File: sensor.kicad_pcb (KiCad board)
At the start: 2 copper layers, 62 x 58.5 mm, 7 parts, among them U1 ESP-12F

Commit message: Schematic finishing and cleanup.
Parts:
- renumbered REF** to CON1, U1 to U3, REF** to U5
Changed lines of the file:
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@@
     (tags "Micro-USB SMD Typ-B")
     (attr smd)
-    (fp_text reference REF** (at 0 -3.1125) (layer F.SilkS)
+    (fp_text reference CON1 (at 0 -3.1125) (layer F.SilkS)
       (effects (font (size 1 1) (thickness 0.15)))
     )
@@
     (tags "Wi-Fi Module")
     (attr smd)
-    (fp_text reference U1 (at -10.56 -5.26) (layer F.SilkS)
+    (fp_text reference U3 (at -10.56 -5.26) (layer F.SilkS)
       (effects (font (size 1 1) (thickness 0.15)))
     )
@@
     (descr "Through hole straight socket strip, 2x05, 1.27mm pitch, double cols (from Kicad 4.0.7), script generated")
     (tags "Through hole socket strip THT 2x05 1.27mm double row")
-    (fp_text reference REF** (at 0 8.89) (layer B.SilkS)
+    (fp_text reference U5 (at 0 8.89) (layer B.SilkS)
       (effects (font (size 1 1) (thickness 0.15)) (justify mirror))
     )

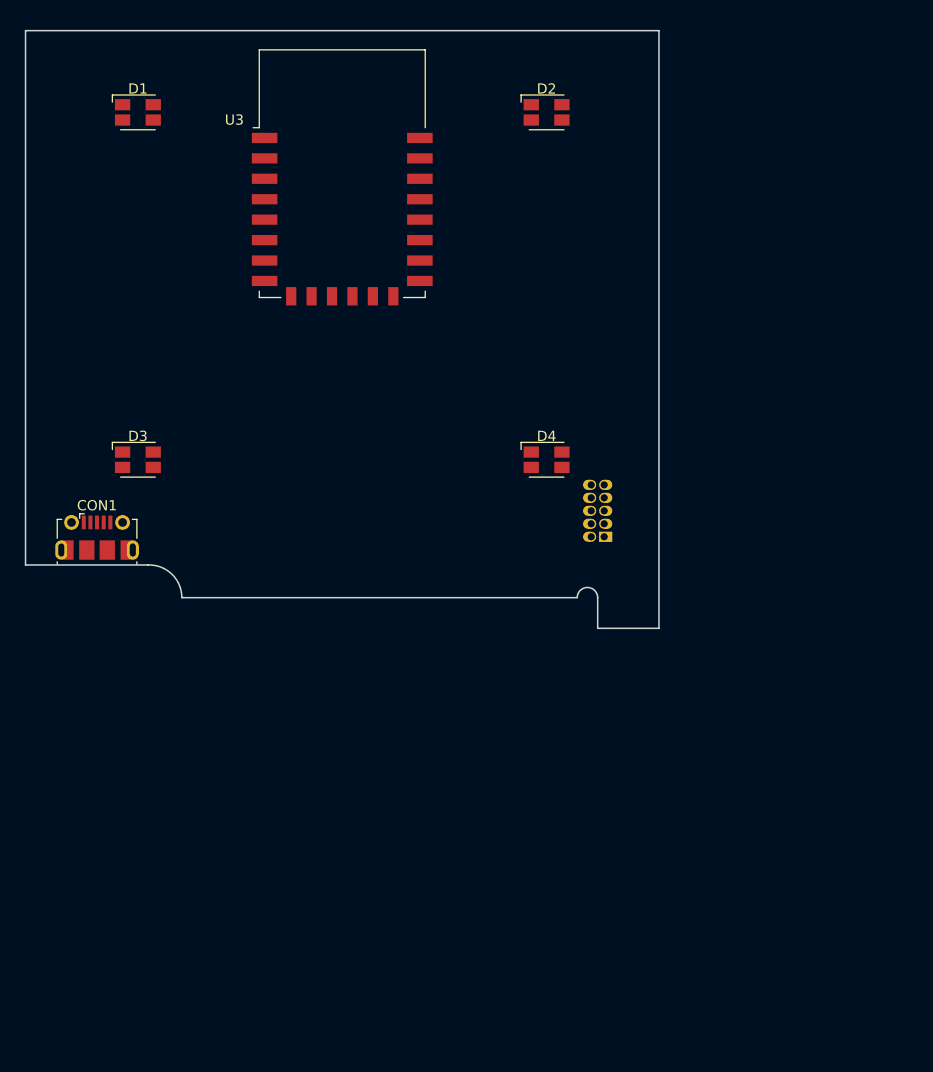
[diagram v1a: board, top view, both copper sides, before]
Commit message: Initial draft PCB placement
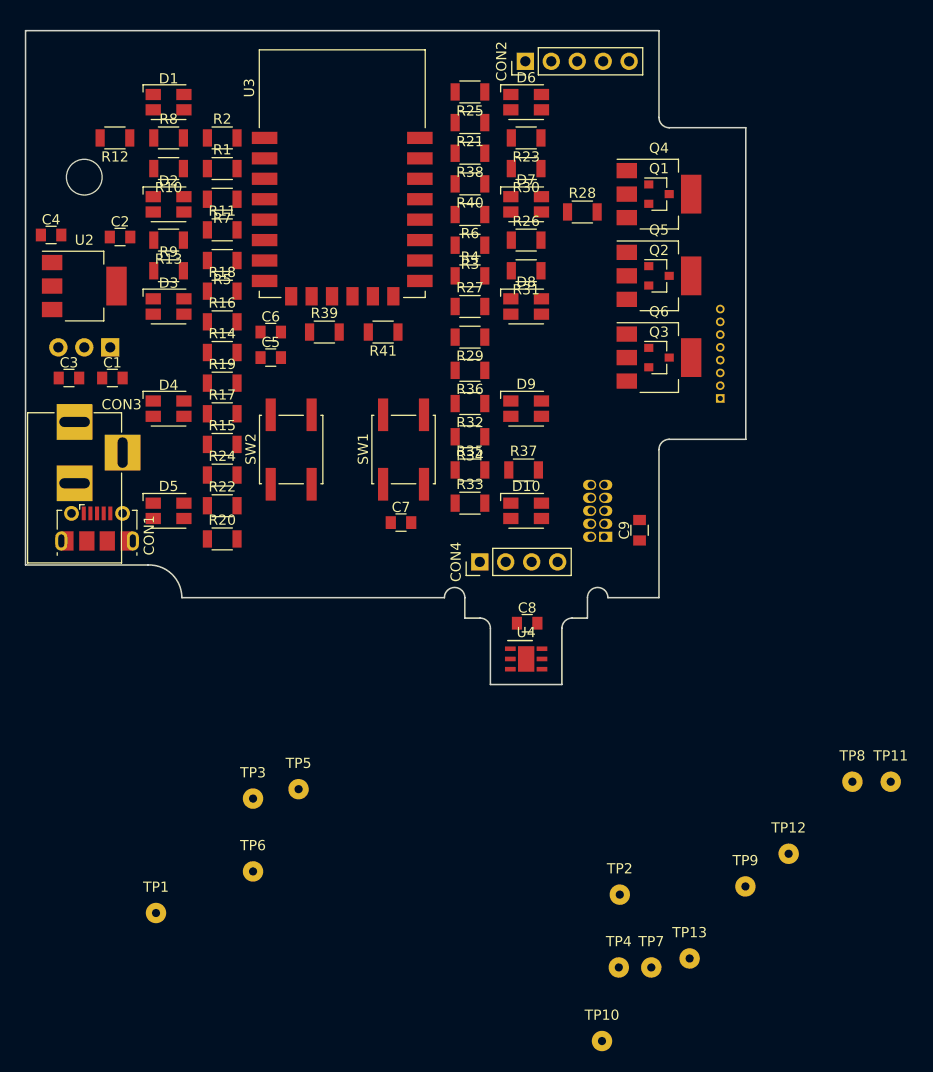
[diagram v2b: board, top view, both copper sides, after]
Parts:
- added C1: 1uF/25V, Capacitors_SMD:C_0805, F.Cu at (74.5, 76.0)
- added C2: 10uF/10V, Capacitors_SMD:C_0805, F.Cu at (75.2, 62.2)
- added C3: 100nF, Capacitors_SMD:C_0805, F.Cu at (70.2, 76.0)
- added C4: 10uF/10V, Capacitors_SMD:C_0805, F.Cu at (68.5, 62.0)
- added C5: 10uF/10V, Capacitors_SMD:C_0805, F.Cu at (90.0, 74.0)
- added C6: 100nF, Capacitors_SMD:C_0805, F.Cu at (90.0, 71.5)
- added C7: 100nF, Capacitors_SMD:C_0805, F.Cu at (102.8, 90.2)
- added C8: 100nF, Capacitors_SMD:C_0805, F.Cu at (115.1, 100.0)
- added C9: 10uF/10V, Capacitors_SMD:C_0805, F.Cu at (126.1, 90.9)
- added CON2: PROG, Pin_Headers:Pin_Header_Straight_1x05_Pitch2.54mm, F.Cu at (114.9, 45.0)
- added CON3: Jack-DC, Connectors:BARREL_JACK, F.Cu at (70.8, 80.3)
- added CON4: HTU21D, Pin_Headers:Pin_Header_Straight_1x04_Pitch2.54mm, F.Cu at (110.5, 94.0)
- added CON5: Conn_01x08, Connectors_Molex:Molex_PicoBlade_53048-0810_08x1.25mm_Angled, B.Cu at (134.0, 78.0)
- added D10: ASMB-MTB0-0A3A2, less-smog:ASMB-MTB0-0A3A2, F.Cu at (115.0, 89.0)
- added D5: ASMB-MTB0-0A3A2, less-smog:ASMB-MTB0-0A3A2, F.Cu at (80.0, 89.0)
- added D6: ASMB-MTB0-0A3A2, less-smog:ASMB-MTB0-0A3A2, F.Cu at (115.0, 49.0)
- added D7: ASMB-MTB0-0A3A2, less-smog:ASMB-MTB0-0A3A2, F.Cu at (115.0, 59.0)
- added D8: ASMB-MTB0-0A3A2, less-smog:ASMB-MTB0-0A3A2, F.Cu at (115.0, 69.0)
- added D9: ASMB-MTB0-0A3A2, less-smog:ASMB-MTB0-0A3A2, F.Cu at (115.0, 79.0)
- added Q1: BSS214N, TO_SOT_Packages_SMD:SOT-23, F.Cu at (128.0, 58.0)
- added Q2: BSS214N, TO_SOT_Packages_SMD:SOT-23, F.Cu at (128.0, 66.0)
- added Q3: BSS214N, TO_SOT_Packages_SMD:SOT-23, F.Cu at (128.0, 74.0)
- added Q4: BSS214N, TO_SOT_Packages_SMD:SOT-223-3Lead_TabPin2, F.Cu at (128.0, 58.0)
- added Q5: BSS214N, TO_SOT_Packages_SMD:SOT-223-3Lead_TabPin2, F.Cu at (128.0, 66.0)
- added Q6: BSS214N, TO_SOT_Packages_SMD:SOT-223-3Lead_TabPin2, F.Cu at (128.0, 74.0)
- added R1: 10k, Resistors_SMD:R_1206, F.Cu at (85.2, 55.5)
- added R10: 130, Resistors_SMD:R_1206, F.Cu at (80.0, 55.5)
- added R11: 130, Resistors_SMD:R_1206, F.Cu at (85.2, 61.5)
- added R12: 130, Resistors_SMD:R_1206, F.Cu at (74.8, 52.5)
- added R13: 130, Resistors_SMD:R_1206, F.Cu at (80.0, 62.5)
- added R14: 180, Resistors_SMD:R_1206, F.Cu at (85.2, 73.5)
- added R15: 180, Resistors_SMD:R_1206, F.Cu at (85.2, 82.5)
- added R16: 130, Resistors_SMD:R_1206, F.Cu at (85.2, 70.5)
- added R17: 130, Resistors_SMD:R_1206, F.Cu at (85.2, 79.5)
- added R18: 130, Resistors_SMD:R_1206, F.Cu at (85.2, 67.5)
- added R19: 130, Resistors_SMD:R_1206, F.Cu at (85.2, 76.5)
- added R2: 10k, Resistors_SMD:R_1206, F.Cu at (85.2, 52.5)
- added R20: 180, Resistors_SMD:R_1206, F.Cu at (85.2, 91.8)
- added R21: 180, Resistors_SMD:R_1206, F.Cu at (109.5, 51.0)
- added R22: 130, Resistors_SMD:R_1206, F.Cu at (85.2, 88.5)
- added R23: 130, Resistors_SMD:R_1206, F.Cu at (115.0, 52.5)
- added R24: 130, Resistors_SMD:R_1206, F.Cu at (85.2, 85.5)
- added R25: 130, Resistors_SMD:R_1206, F.Cu at (109.5, 48.0)
- added R26: 180, Resistors_SMD:R_1206, F.Cu at (115.0, 62.5)
- added R27: 180, Resistors_SMD:R_1206, F.Cu at (109.5, 69.0)
- added R28: 130, Resistors_SMD:R_1206, F.Cu at (120.5, 59.8)
- added R29: 130, Resistors_SMD:R_1206, F.Cu at (109.5, 72.0)
- added R3: 10k, Resistors_SMD:R_1206, F.Cu at (109.5, 63.0)
- added R30: 130, Resistors_SMD:R_1206, F.Cu at (115.0, 55.5)
- added R31: 130, Resistors_SMD:R_1206, F.Cu at (115.0, 65.5)
- added R32: 180, Resistors_SMD:R_1206, F.Cu at (109.5, 78.5)
- added R33: 180, Resistors_SMD:R_1206, F.Cu at (109.5, 88.2)
- added R34: 130, Resistors_SMD:R_1206, F.Cu at (109.5, 81.8)
- added R35: 130, Resistors_SMD:R_1206, F.Cu at (109.5, 85.0)
- added R36: 130, Resistors_SMD:R_1206, F.Cu at (109.5, 75.2)
- added R37: 130, Resistors_SMD:R_1206, F.Cu at (114.8, 85.0)
- added R38: 10k, Resistors_SMD:R_1206, F.Cu at (109.5, 54.0)
- added R39: 10k, Resistors_SMD:R_1206, F.Cu at (95.2, 71.5)
- added R4: 10k, Resistors_SMD:R_1206, F.Cu at (109.5, 66.0)
- added R40: 10k, Resistors_SMD:R_1206, F.Cu at (109.5, 57.0)
- added R41: 10k, Resistors_SMD:R_1206, F.Cu at (101.0, 71.5)
- added R5: 10k, Resistors_SMD:R_1206, F.Cu at (85.2, 64.5)
- added R6: 10k, Resistors_SMD:R_1206, F.Cu at (109.5, 60.0)
- added R7: 10k, Resistors_SMD:R_1206, F.Cu at (85.2, 58.5)
- added R8: 180, Resistors_SMD:R_1206, F.Cu at (80.0, 52.5)
- added R9: 180, Resistors_SMD:R_1206, F.Cu at (80.0, 65.5)
- added SW1: RESET, Buttons_Switches_SMD:SW_SPST_EVQQ2, F.Cu at (103.0, 83.0)
- added SW2: CFG, Buttons_Switches_SMD:SW_SPST_EVQQ2, F.Cu at (92.0, 83.0)
- added TP1: ESP_PD, Wire_Pads:SolderWirePad_single_0-8mmDrill, F.Cu at (78.8, 128.4)
- added TP10: -, Wire_Pads:SolderWirePad_single_0-8mmDrill, F.Cu at (122.4, 140.9)
- added TP11: -, Wire_Pads:SolderWirePad_single_0-8mmDrill, F.Cu at (150.7, 115.5)
- added TP12: -, Wire_Pads:SolderWirePad_single_0-8mmDrill, F.Cu at (140.7, 122.6)
- added TP13: +3V3, Wire_Pads:SolderWirePad_single_0-8mmDrill, F.Cu at (131.0, 132.8)
- added TP2: GND, Wire_Pads:SolderWirePad_single_0-8mmDrill, F.Cu at (124.2, 126.6)
- added TP3: -, Wire_Pads:SolderWirePad_single_0-8mmDrill, F.Cu at (88.3, 117.2)
- added TP4: CFG, Wire_Pads:SolderWirePad_single_0-8mmDrill, F.Cu at (124.1, 133.7)
- added TP5: RESET, Wire_Pads:SolderWirePad_single_0-8mmDrill, F.Cu at (92.7, 116.2)
- added TP6: -, Wire_Pads:SolderWirePad_single_0-8mmDrill, F.Cu at (88.3, 124.3)
- added TP7: -, Wire_Pads:SolderWirePad_single_0-8mmDrill, F.Cu at (127.2, 133.7)
- added TP8: +5V, Wire_Pads:SolderWirePad_single_0-8mmDrill, F.Cu at (146.9, 115.5)
- added TP9: +12V, Wire_Pads:SolderWirePad_single_0-8mmDrill, F.Cu at (136.5, 125.8)
- added U1: LM7805, TO_SOT_Packages_THT:TO-220_Horizontal, B.Cu at (74.3, 73.0)
- added U2: TLV1117LV33DCY, TO_SOT_Packages_SMD:SOT-223-3Lead_TabPin2, F.Cu at (71.8, 67.0)
- added U4: HTU21D, less-smog:HTU21D, F.Cu at (115.0, 103.5)
- CON1: value USB_Micro-B_Molex-105017-0001 -> Micro USB; footprint Connector_USB:USB_Micro-B_Molex-105017-0001 -> Connectors_USB:USB_Micro-B_Molex-105017-0001
- D1, D2, D3, D4: value RGB -> ASMB-MTB0-0A3A2
- U3: footprint RF_Modules:ESP-12E -> less-smog:ESP-12F
- moved D2 38.1 mm to (80.0, 59.0)
- moved D4 37.3 mm to (80.0, 79.0)
- moved D3 15.3 mm to (80.0, 69.0)
- moved D1 3.16 mm to (80.0, 49.0)
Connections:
- CON1 pad 1: (no net) -> +5V
- CON1 pad 2: (no net) -> Net-(CON1-Pad2)
- CON1 pad 3: (no net) -> Net-(CON1-Pad3)
- CON1 pad 4: (no net) -> Net-(CON1-Pad4)
- CON1 pad 5: (no net) -> GND
- CON1 pad 6: (no net) -> GND
- D1 pad 1: (no net) -> +5V
- D1 pad 2: (no net) -> Net-(D1-Pad2)
- D1 pad 3: (no net) -> Net-(D1-Pad3)
- D1 pad 4: (no net) -> Net-(D1-Pad4)
- D2 pad 1: (no net) -> +5V
- D2 pad 2: (no net) -> Net-(D2-Pad2)
- D2 pad 3: (no net) -> Net-(D2-Pad3)
- D2 pad 4: (no net) -> Net-(D2-Pad4)
- D3 pad 1: (no net) -> +5V
- D3 pad 2: (no net) -> Net-(D3-Pad2)
- D3 pad 3: (no net) -> Net-(D3-Pad3)
- D3 pad 4: (no net) -> Net-(D3-Pad4)
- D4 pad 1: (no net) -> +5V
- D4 pad 2: (no net) -> Net-(D4-Pad2)
- D4 pad 3: (no net) -> Net-(D4-Pad3)
- D4 pad 4: (no net) -> Net-(D4-Pad4)
- U3 pad 1: Net-(U1-Pad1) -> RESET
- U3 pad 11: Net-(U1-Pad11) -> PMS_SET
- U3 pad 12: Net-(U1-Pad12) -> PMS_RESET
- U3 pad 15: Net-(U1-Pad15) -> GND
- U3 pad 16: Net-(U1-Pad16) -> LED_G_CTRL
- U3 pad 17: Net-(U1-Pad17) -> /BOOT1
- U3 pad 18: Net-(U1-Pad18) -> CFG_BTN
- U3 pad 19: Net-(U1-Pad19) -> HTU_SCL
- U3 pad 20: Net-(U1-Pad20) -> HTU_SDA
- U3 pad 21: Net-(U1-Pad21) -> ESP_RXD
- U3 pad 22: Net-(U1-Pad22) -> ESP_TXD
- U3 pad 3: Net-(U1-Pad3) -> /ESP_PD
- U3 pad 4: Net-(U1-Pad4) -> LED_B_CTRL
- U3 pad 5: Net-(U1-Pad5) -> PMS_TXD
- U3 pad 6: Net-(U1-Pad6) -> PMS_RXD
- U3 pad 7: Net-(U1-Pad7) -> LED_R_CTRL
- U3 pad 8: Net-(U1-Pad8) -> +3V3
- U5 pad 1: (no net) -> +5V
- U5 pad 10: (no net) -> PMS_SET
- U5 pad 2: (no net) -> +5V
- U5 pad 3: (no net) -> GND
- U5 pad 4: (no net) -> GND
- U5 pad 5: (no net) -> PMS_RESET
- U5 pad 7: (no net) -> PMS_RXD
- U5 pad 9: (no net) -> PMS_TXD
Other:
- board size 62 x 58.5 mm -> 70.5 x 64 mm

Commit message: Change some footprint pads to bigger ones.
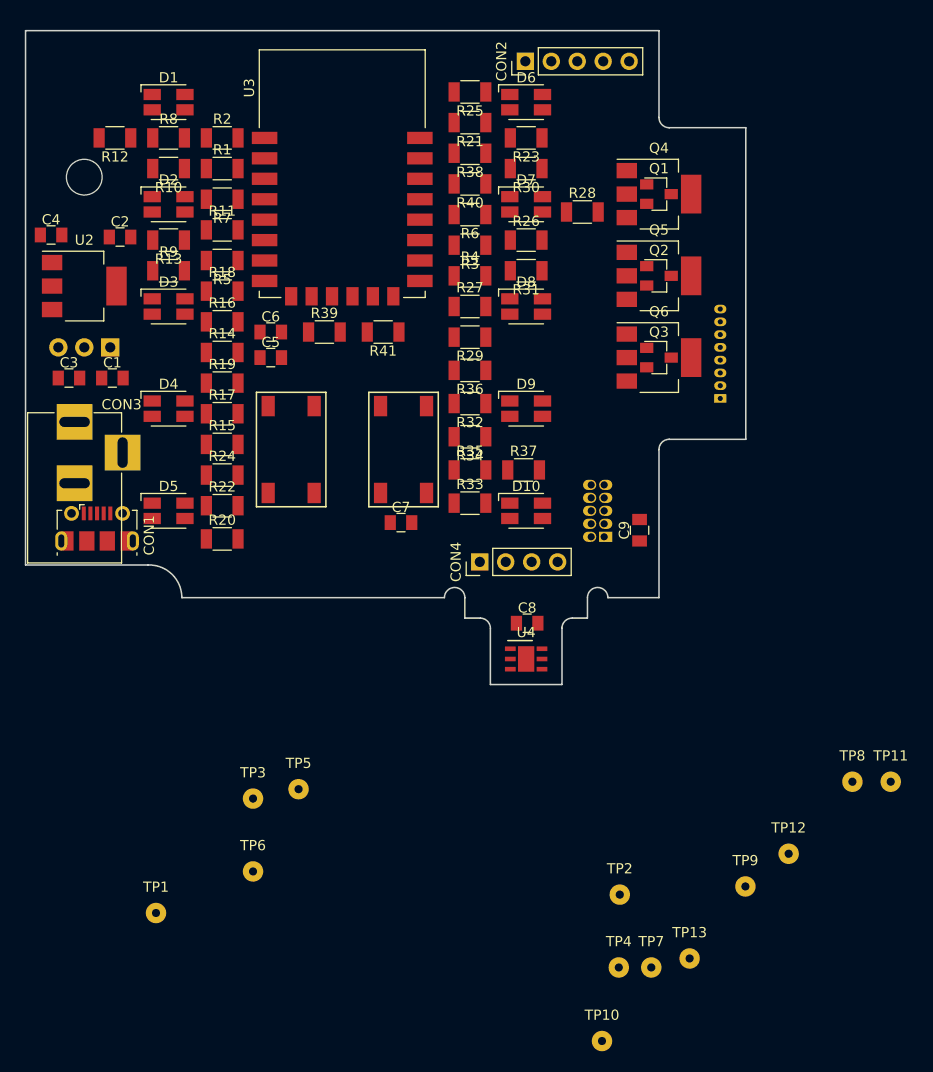
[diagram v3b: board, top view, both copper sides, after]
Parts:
- C1, C2, C3, C4, C5, C6, C7, C8, C9: footprint Capacitors_SMD:C_0805 -> less-smog:C_0805
- CON5: footprint Connectors_Molex:Molex_PicoBlade_53048-0810_08x1.25mm_Angled -> less-smog:Molex_PicoBlade_53048-0810
- Q1, Q2, Q3: footprint TO_SOT_Packages_SMD:SOT-23 -> less-smog:SOT-23
- R1, R10, R11, R12, R13, R14, R15, R16, R17, R18, R19, R2, R20, R21, R22, R23, R24, R25, R26, R27, R28, R29, R3, R30, R31, R32, R33, R34, R35, R36, R37, R38, R39, R4, R40, R41, R5, R6, R7, R8, R9: footprint Resistors_SMD:R_1206 -> less-smog:R_1206
- SW1, SW2: footprint Buttons_Switches_SMD:SW_SPST_EVQQ2 -> less-smog:MicroswitchSmd-4.3_N
- turned SW1 to 180 degrees
- turned SW2 to 180 degrees

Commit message: Add HTU21D module footprint
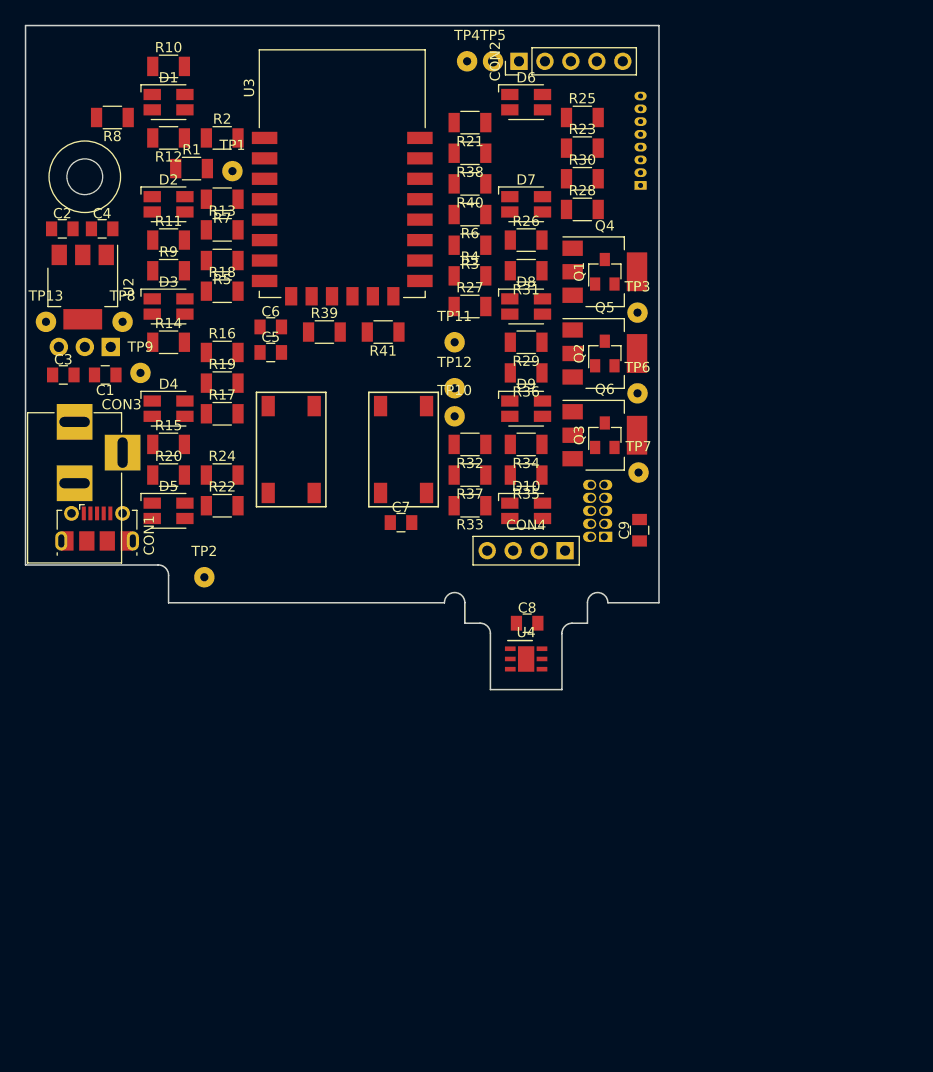
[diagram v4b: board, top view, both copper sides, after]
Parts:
- CON4: footprint Pin_Headers:Pin_Header_Straight_1x04_Pitch2.54mm -> less-smog:HTU21D_module
- moved TP4 89.9 mm to (109.2, 45.0)
- moved TP13 88.6 mm to (68.0, 70.5)
- moved TP8 84.4 mm to (75.5, 70.5)
- moved TP9 77.7 mm to (77.2, 75.5)
- moved TP5 73.7 mm to (111.8, 45.0)
- moved TP1 73.0 mm to (86.2, 55.8)
- moved TP10 62.8 mm to (108.0, 79.8)
- moved TP3 60.7 mm to (125.9, 69.6)
- moved TP11 60.6 mm to (108.0, 72.5)
- moved TP6 60.1 mm to (125.9, 77.5)
- moved TP12 56.1 mm to (108.0, 77.0)
- moved TP2 51.2 mm to (83.5, 95.5)
- moved TP7 48.5 mm to (126.0, 85.2)
- moved CON5 22.3 mm to (126.2, 57.1)
- moved R25 11.3 mm to (120.5, 50.5), turned to 0 degrees
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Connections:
- CON4 pad 1: HTU_SCL -> +3V3
- CON4 pad 2: HTU_SDA -> GND
- CON4 pad 3: GND -> HTU_SDA
- CON4 pad 4: +3V3 -> HTU_SCL
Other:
- board size 70.5 x 64 mm -> 62 x 65 mm
- net class Default: trace_width 0.25 -> 0.2; via_dia 0.6 -> 0.7
- rule via_min_drill: 0.3 -> 0.4
- rule via_min_size: 0.4 -> 0.7

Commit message: Routing in progress
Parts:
- moved TP7 42.4 mm to (83.6, 85.4)
- moved Q1 37.5 mm to (97.7, 93.5), turned to 0 degrees
- moved Q4 37.5 mm to (97.7, 93.5)
- moved Q3 36.9 mm to (87.8, 93.5), turned to 0 degrees
- moved Q6 36.9 mm to (87.8, 93.5)
- moved TP3 36.6 mm to (94.5, 88.5)
- moved TP6 31.9 mm to (94.0, 78.5)
- moved Q2 27.5 mm to (97.0, 83.5), turned to 0 degrees
- moved Q5 27.5 mm to (97.0, 83.5)
- moved TP12 20.5 mm to (91.0, 88.5)
- moved TP10 11.2 mm to (101.0, 88.5)
- moved R32 10.5 mm to (109.5, 72.0)
- moved TP11 10.0 mm to (100.0, 78.5)
- moved TP13 7.80 mm to (75.8, 70.6)
- moved TP8 7.80 mm to (67.7, 70.6)
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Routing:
- net /LED_G: track 0.00 -> 100.5 mm
- net /LED_B: track 0.00 -> 81.5 mm
- net GND: track 0.00 -> 77.3 mm, vias 0 -> 13
- net +3V3: track 0.00 -> 72.0 mm, vias 0 -> 1
- net /LED_R: track 0.00 -> 62.3 mm
- net +5V: track 0.00 -> 61.9 mm
- net RESET: track 0.00 -> 42.2 mm
- net ESP_RXD: track 0.00 -> 20.0 mm
- net HTU_SDA: track 0.00 -> 19.9 mm
- net HTU_SCL: track 0.00 -> 17.2 mm
- net ESP_TXD: track 0.00 -> 16.6 mm
- net +12V: track 0.00 -> 12.4 mm
- net CFG_BTN: track 0.00 -> 12.1 mm
- net LED_B_CTRL: track 0.00 -> 11.6 mm
- net Net-(D4-Pad3): track 0.00 -> 11.5 mm
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- added copper zone on B.Cu, net GND
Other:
- net class Power added: clearance 0.2, trace_width 0.3, via_dia 0.7, via_drill 0.4
